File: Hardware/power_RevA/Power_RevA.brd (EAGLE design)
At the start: 50 x 50 mm, 11 parts, among them Q401 TIP120

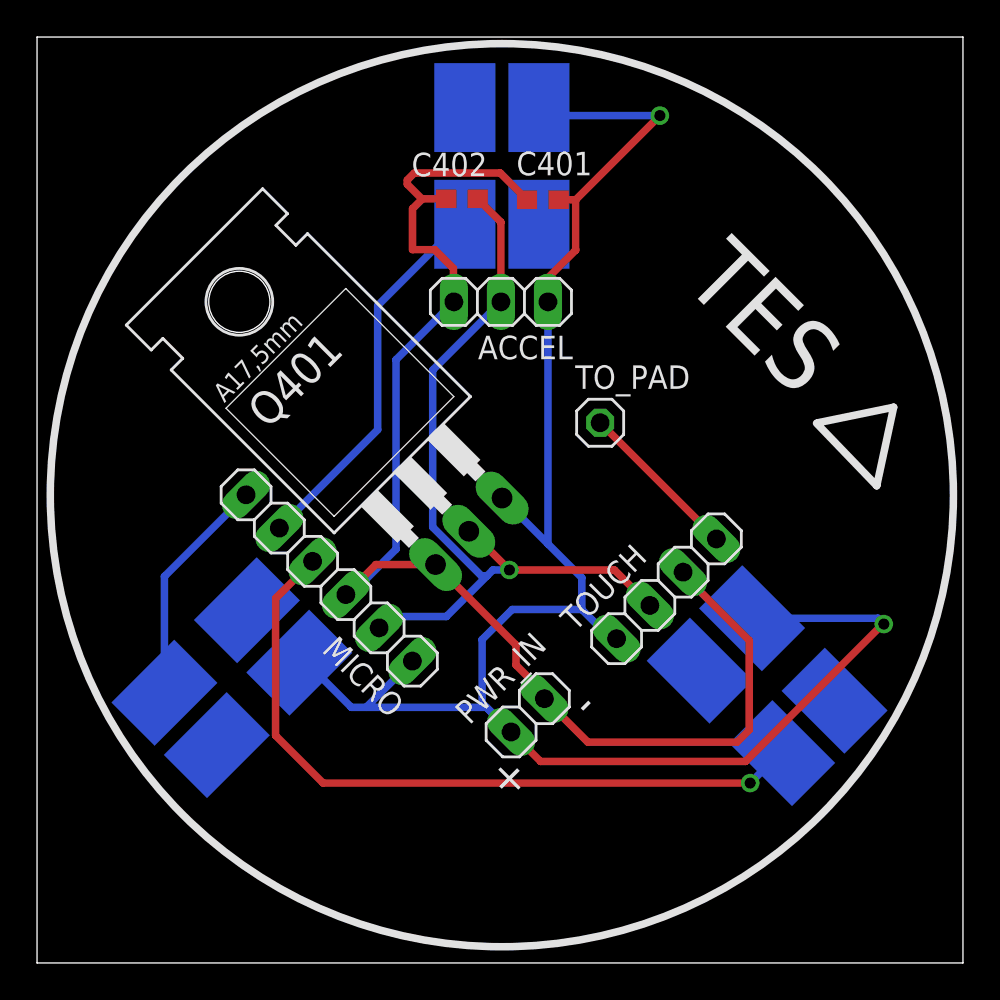
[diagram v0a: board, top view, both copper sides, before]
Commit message: Added Javen's logo to everything
Still need to add plus/minus on leds before order.
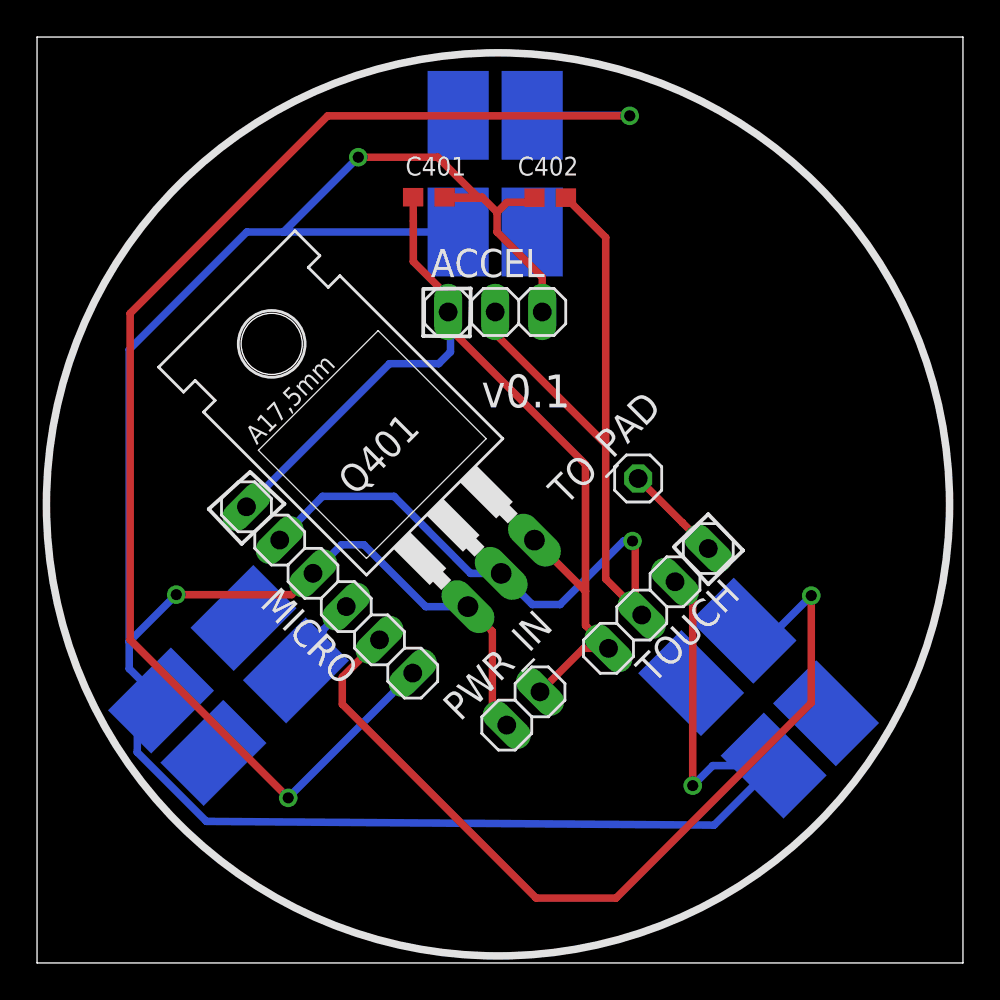
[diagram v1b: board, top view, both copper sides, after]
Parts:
- moved LED2 31.9 mm to (39.0, 14.3), turned to 315 degrees
- moved LED1 30.7 mm to (24.7, 42.6), turned to 0 degrees
- moved LED3 29.1 mm to (10.3, 15.0), turned to 45 degrees
- moved C401 6.15 mm to (21.2, 41.4), turned to 180 degrees
- moved C402 4.77 mm to (27.7, 41.3)
- moved TO_PAD 3.64 mm to (32.5, 26.2)
- moved Q401 2.87 mm to (20.6, 25.5)
- moved TOUCH 0.68 mm to (33.6, 19.7)
- moved MICRO 0.65 mm to (15.8, 20.1), turned to 315 degrees
- moved ACCEL 0.63 mm to (24.7, 35.2), turned to 0 degrees
- moved PWR_IN 0.44 mm to (26.3, 13.7), turned to 225 degrees
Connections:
- removed net N$3: LED1.C@4, MICRO.6
- new net N$7: LED1.A, MICRO.6
- net N$2: no longer LED1.A, LED2.A, LED3.A
- net N$5: now also LED3.A, MICRO.4; no longer LED2.C@4, MICRO.5
- net N$6: now also LED2.A, MICRO.5; no longer LED3.C@4, MICRO.4
- net N$8: now also LED1.C@4, LED2.C@4, LED3.C@4
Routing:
- net N$8: track 73.2 -> 153.6 mm, vias 0 -> 3
- net N$7: track 0.00 -> 75.9 mm, vias 0 -> 2
- net N$2: track 102.9 -> 54.4 mm, vias 2 -> 0
- net N$4: track 43.6 -> 61.4 mm
- net N$5: track 20.7 -> 4.57 mm
- net N$3: track 12.5 -> 0.00 mm
- net N$6: track 39.3 -> 48.6 mm
- net N$1: track 8.87 -> 5.35 mm
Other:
- board text added: "v0.1"
- board text removed: "+"
- board text removed: "-"
- board text removed: "TES"

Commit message: Update of hw files
Added logo to brds, added +/- to LEDs and generated and updated gerber
files.
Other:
- outline, holes or cut-outs redrawn
- board text added: "+"
- board text added: "-"
